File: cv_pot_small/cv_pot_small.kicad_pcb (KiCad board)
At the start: 2 copper layers, 24 x 17 mm, 13 parts, among them J1 I/O connector, U1 HT7550-1, U2 LMV321IDBVR

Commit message: Switched to TLV6001UIDBVR Opamp
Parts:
- U2: value LMV321IDBVR -> TLV6001UIDBVR
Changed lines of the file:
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@@
     (descr "SOT, 5 Pin (https://www.jedec.org/sites/default/files/docs/Mo-178c.PDF variant AA), generated with kicad-footprint-generator ipc_gullwing_generator.py")
     (tags "SOT TO_SOT_SMD")
-    (property "LCSC" "C7972")
+    (property "LCSC" "")
     (property "Sheetfile" "cv_pot_small.kicad_sch")
     (property "Sheetname" "")
@@
       (effects (font (size 1 1) (thickness 0.15)))
     )
-    (fp_text value "LMV321IDBVR" (at 0 2.4 90) (layer "F.Fab")
+    (fp_text value "TLV6001UIDBVR" (at 0 2.4 90) (layer "F.Fab")
       (effects (font (size 1 1) (thickness 0.15)))
     )

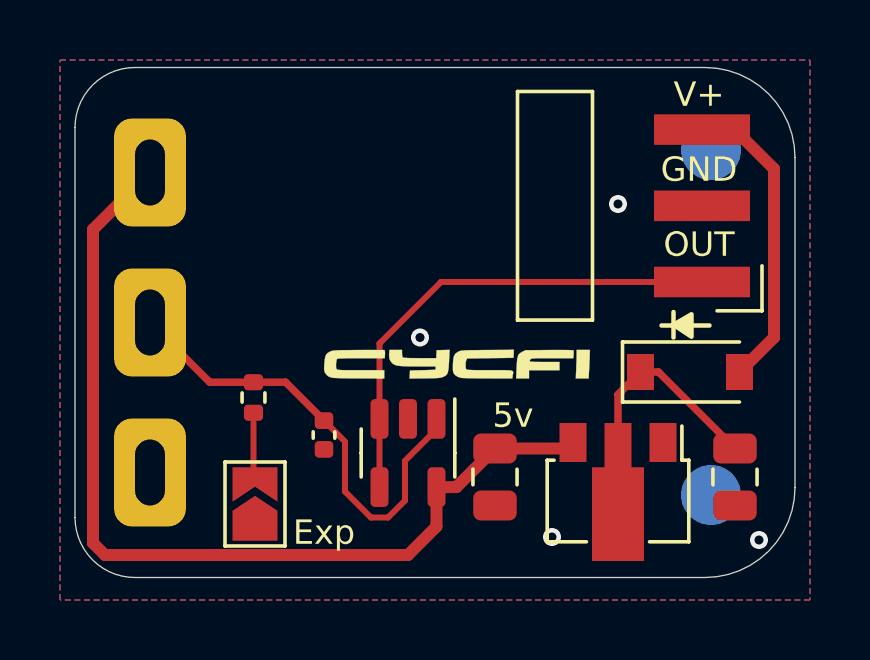
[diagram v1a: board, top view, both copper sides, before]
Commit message: Changed taper resistor value
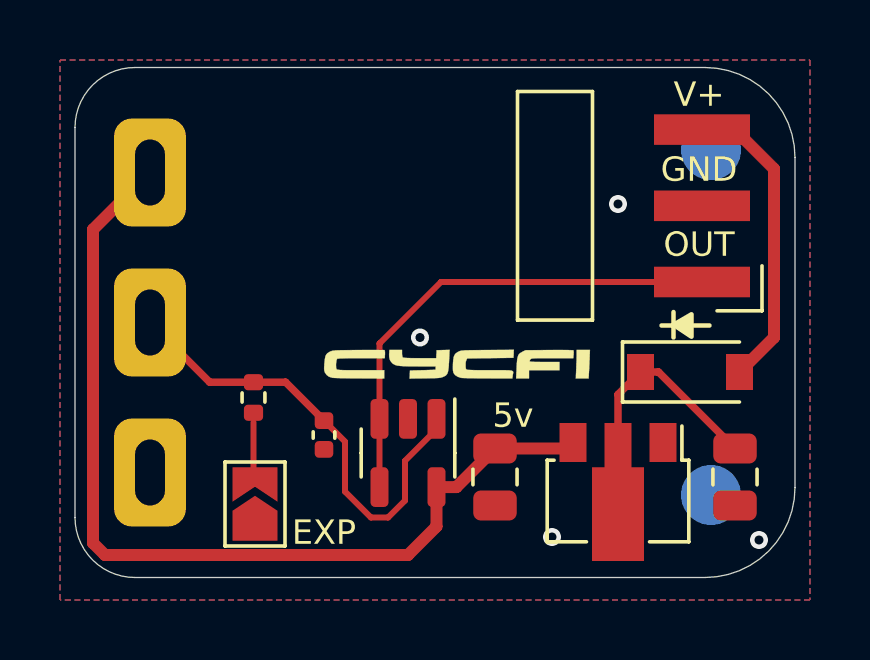
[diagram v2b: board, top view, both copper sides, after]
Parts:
- R1: value 4.7k -> 47k
- RV1: value 25k -> 250k
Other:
- board text added: "EXP"
- board text removed: "Exp"
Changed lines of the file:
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@@
   (footprint "cycfi_library:bourns_pdb181" (layer "F.Cu")
     (at 139.5 75.5)
-    (property "Sheetfile" "cv_pot_small.kicad_sch")
+    (property "Sheetfile" "File: cv_pot_small.kicad_sch")
     (property "Sheetname" "")
     (attr smd)
@@
       (effects (font (size 1 1) (thickness 0.15)))
     )
-    (fp_text value "25k" (at 0 15 unlocked) (layer "F.Fab")
+    (fp_text value "250k" (at 0 15 unlocked) (layer "F.Fab")
       (effects (font (size 1 1) (thickness 0.15)))
     )
@@
   (footprint "cycfi_library:pin_header_1x3p_2.54mm_smd_horizontal" (layer "F.Cu")
     (at 157.9 79.15 180)
-    (property "Sheetfile" "cv_pot_small.kicad_sch")
+    (property "Sheetfile" "File: cv_pot_small.kicad_sch")
     (property "Sheetname" "")
     (attr through_hole)
@@
     (descr "SOT, 5 Pin (https://www.jedec.org/sites/default/files/docs/Mo-178c.PDF variant AA), generated with kicad-footprint-generator ipc_gullwing_generator.py")
     (tags "SOT TO_SOT_SMD")
-    (property "LCSC" "")
-    (property "Sheetfile" "cv_pot_small.kicad_sch")
+    (property "JLCPCB_CORRECTION" "0;0;180")
+    (property "LCSC" "C544299")
+    (property "Sheetfile" "File: cv_pot_small.kicad_sch")
     (property "Sheetname" "")
     (attr smd)
@@
     (tags "capacitor")
     (property "LCSC" "C15850")
-    (property "Sheetfile" "cv_pot_small.kicad_sch")
+    (property "Sheetfile" "File: cv_pot_small.kicad_sch")
     (property "Sheetname" "")
     (attr smd)
@@
     (tags "SOD-123")
     (property "LCSC" "C81598")
-    (property "Sheetfile" "cv_pot_small.kicad_sch")
+    (property "Sheetfile" "File: cv_pot_small.kicad_sch")
     (property "Sheetname" "")
     (attr smd)
@@
     )
   )
-  (footprint "cycfi_library:cycfi-logo-9mm" locked (layer "F.Cu")
+  (footprint "cycfi_library:cycfi-logo-9mm" (layer "F.Cu")
     (at 149.7 81.9)
-    (attr through_hole)
+    (attr through_hole board_only)
     (fp_text reference "G***" (at 0 0) (layer "F.SilkS") hide
       (effects (font (size 1.524 1.524) (thickness 0.3)))
@@
     (descr "SOT-89-3, http://ww1.microchip.com/downloads/en/DeviceDoc/3L_SOT-89_MB_C04-029C.pdf")
     (tags "SOT-89-3")
+    (property "JLCPCB_CORRECTION" "0;0;180")
     (property "LCSC" "C16106")
-    (property "Sheetfile" "cv_pot_small.kicad_sch")
+    (property "Sheetfile" "File: cv_pot_small.kicad_sch")
     (property "Sheetname" "")
     (attr smd)
@@
     (descr "Resistor SMD 0402 (1005 Metric), square (rectangular) end terminal, IPC_7351 nominal, (Body size source: IPC-SM-782 page 72, https://www.pcb-3d.com/wordpress/wp-content/uploads/ipc-sm-782a_amendment_1_and_2.pdf), generated with kicad-footprint-generator")
     (tags "resistor")
-    (property "LCSC" "C25900")
-    (property "Sheetfile" "cv_pot_small.kicad_sch")
+    (property "LCSC" "C25792")
+    (property "Sheetfile" "File: cv_pot_small.kicad_sch")
     (property "Sheetname" "")
     (attr smd)
@@
       (effects (font (size 1 1) (thickness 0.15)))
     )
-    (fp_text value "4.7k" (at 0 1.17 -90) (layer "F.Fab")
+    (fp_text value "47k" (at 0 1.17 -90) (layer "F.Fab")
       (effects (font (size 1 1) (thickness 0.15)))
     )
@@
     (tags "capacitor")
     (property "LCSC" "C15850")
-    (property "Sheetfile" "cv_pot_small.kicad_sch")
+    (property "Sheetfile" "File: cv_pot_small.kicad_sch")
     (property "Sheetname" "")
     (attr smd)
@@
     (tags "capacitor")
     (property "LCSC" "C307331")
-    (property "Sheetfile" "cv_pot_small.kicad_sch")
+    (property "Sheetfile" "File: cv_pot_small.kicad_sch")
     (property "Sheetname" "")
     (attr smd)
@@
     (descr "SMD Solder Jumper, 1x1.5mm Triangular Pads, 0.3mm gap, open")
     (tags "solder jumper open")
-    (property "Sheetfile" "cv_pot_small.kicad_sch")
+    (property "Sheetfile" "File: cv_pot_small.kicad_sch")
     (property "Sheetname" "")
     (attr exclude_from_pos_files)
@@
   (footprint "cycfi_library:single-pad-2x2-circular" (layer "B.Cu")
     (at 158.2 74.75 180)
-    (property "Sheetfile" "cv_pot_small.kicad_sch")
+    (property "Sheetfile" "File: cv_pot_small.kicad_sch")
     (property "Sheetname" "")
     (attr through_hole)
@@
   (footprint "cycfi_library:single-pad-2x2-circular" (layer "B.Cu")
     (at 158.2 86.25 180)
-    (property "Sheetfile" "cv_pot_small.kicad_sch")
+    (property "Sheetfile" "File: cv_pot_small.kicad_sch")
     (property "Sheetname" "")
     (attr through_hole)
@@
   (gr_line (start 158 89) (end 139 89) (layer "Edge.Cuts") (width 0.0381))
   (gr_arc (start 137 74) (mid 137.585786 72.585786) (end 139 72) (layer "Edge.Cuts") (width 0.0381))
-  (gr_text "Exp" (at 145.3 87.5) (layer "F.SilkS")
+  (gr_text "EXP" (at 145.3 87.5) (layer "F.SilkS")
     (effects (font (size 0.8128 0.8128) (thickness 0.1524)))
   )

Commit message: Added 1k output resistor
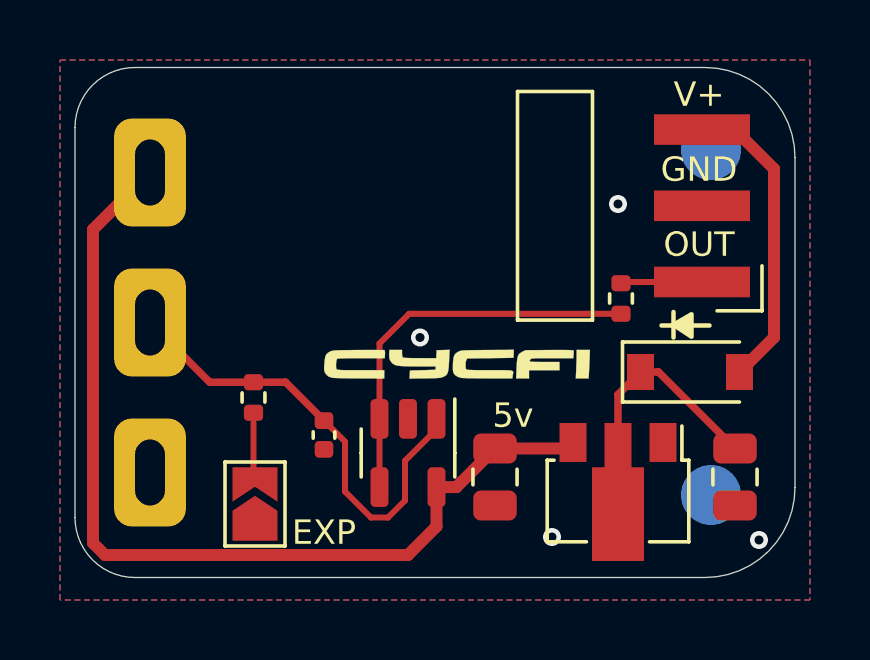
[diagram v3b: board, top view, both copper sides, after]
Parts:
- added R2: 1k, Resistor_SMD:R_0402_1005Metric, F.Cu at (155.2, 79.7)
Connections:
- U2 pad 3: OUT -> Net-(U2-Pad3)
- U2 pad 4: OUT -> Net-(U2-Pad3)
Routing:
- net OUT: track 16.4 -> 2.72 mm
- net Net-(U2-Pad3): track 0.00 -> 13.2 mm
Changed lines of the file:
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@@
   (net 6 "OUT")
   (net 7 "Net-(JP1-Pad2)")
+  (net 8 "Net-(U2-Pad3)")
   (footprint "cycfi_library:bourns_pdb181" (layer "F.Cu")
     (at 139.5 75.5)
@@
       (net 2 "GND") (pinfunction "V-") (pintype "power_in"))
     (pad "3" smd roundrect (at -1.1375 0.95 270) (size 1.325 0.6) (layers "F.Cu" "F.Paste" "F.Mask") (roundrect_rratio 0.25)
-      (net 6 "OUT") (pinfunction "-") (pintype "input"))
+      (net 8 "Net-(U2-Pad3)") (pinfunction "-") (pintype "input"))
     (pad "4" smd roundrect (at 1.1375 0.95 270) (size 1.325 0.6) (layers "F.Cu" "F.Paste" "F.Mask") (roundrect_rratio 0.25)
-      (net 6 "OUT") (pintype "output"))
+      (net 8 "Net-(U2-Pad3)") (pintype "output"))
     (pad "5" smd roundrect (at 1.1375 -0.95 270) (size 1.325 0.6) (layers "F.Cu" "F.Paste" "F.Mask") (roundrect_rratio 0.25)
       (net 3 "5v") (pinfunction "V+") (pintype "power_in"))
@@
     )
   )
+  (footprint "Resistor_SMD:R_0402_1005Metric" (layer "F.Cu")
+    (at 155.2 79.7 90)
+    (descr "Resistor SMD 0402 (1005 Metric), square (rectangular) end terminal, IPC_7351 nominal, (Body size source: IPC-SM-782 page 72, https://www.pcb-3d.com/wordpress/wp-content/uploads/ipc-sm-782a_amendment_1_and_2.pdf), generated with kicad-footprint-generator")
+    (tags "resistor")
+    (property "LCSC" "C11702")
+    (property "Sheetfile" "File: cv_pot_small.kicad_sch")
+    (property "Sheetname" "")
+    (attr smd)
+    (fp_text reference "R2" (at 0 -1.17 90) (layer "F.SilkS") hide
+      (effects (font (size 1 1) (thickness 0.15)))
+    )
+    (fp_text value "1k" (at 0 1.17 90) (layer "F.Fab")
+      (effects (font (size 1 1) (thickness 0.15)))
+    )
+    (fp_text user "${REFERENCE}" (at 0 0 90) (layer "F.Fab")
+      (effects (font (size 0.26 0.26) (thickness 0.04)))
+    )
+    (fp_line (start -0.153641 0.38) (end 0.153641 0.38) (layer "F.SilkS") (width 0.12))
+    (fp_line (start -0.153641 -0.38) (end 0.153641 -0.38) (layer "F.SilkS") (width 0.12))
+    (fp_line (start 0.93 0.47) (end -0.93 0.47) (layer "F.CrtYd") (width 0.05))
+    (fp_line (start -0.93 0.47) (end -0.93 -0.47) (layer "F.CrtYd") (width 0.05))
+    (fp_line (start 0.93 -0.47) (end 0.93 0.47) (layer "F.CrtYd") (width 0.05))
+    (fp_line (start -0.93 -0.47) (end 0.93 -0.47) (layer "F.CrtYd") (width 0.05))
+    (fp_line (start 0.525 0.27) (end -0.525 0.27) (layer "F.Fab") (width 0.1))
+    (fp_line (start 0.525 -0.27) (end 0.525 0.27) (layer "F.Fab") (width 0.1))
+    (fp_line (start -0.525 0.27) (end -0.525 -0.27) (layer "F.Fab") (width 0.1))
+    (fp_line (start -0.525 -0.27) (end 0.525 -0.27) (layer "F.Fab") (width 0.1))
+    (pad "1" smd roundrect (at -0.51 0 90) (size 0.54 0.64) (layers "F.Cu" "F.Paste" "F.Mask") (roundrect_rratio 0.25)
+      (net 8 "Net-(U2-Pad3)") (pintype "passive"))
+    (pad "2" smd roundrect (at 0.51 0 90) (size 0.54 0.64) (layers "F.Cu" "F.Paste" "F.Mask") (roundrect_rratio 0.25)
+      (net 6 "OUT") (pintype "passive"))
+    (model "${KICAD6_3DMODEL_DIR}/Resistor_SMD.3dshapes/R_0402_1005Metric.wrl"
+      (offset (xyz 0 0 0))
+      (scale (xyz 1 1 1))
+      (rotate (xyz 0 0 0))
+    )
+  )
   (footprint "Capacitor_SMD:C_0805_2012Metric" (layer "F.Cu")
     (at 151 85.65 -90)
@@
   (segment (start 160.3 81) (end 159.15 82.15) (width 0.4) (layer "F.Cu") (net 5))
   (segment (start 157.9 74.07) (end 158.99 74.07) (width 0.4) (layer "F.Cu") (net 5))
-  (segment (start 147.15 85.9875) (end 147.15 83.7125) (width 0.2) (layer "F.Cu") (net 6))
-  (segment (start 147.15 81.2) (end 149.2 79.15) (width 0.2) (layer "F.Cu") (net 6))
-  (segment (start 147.15 83.7125) (end 147.15 81.2) (width 0.2) (layer "F.Cu") (net 6))
-  (segment (start 149.2 79.15) (end 157.9 79.15) (width 0.2) (layer "F.Cu") (net 6))
+  (segment (start 157.9 79.15) (end 155.24 79.15) (width 0.2032) (layer "F.Cu") (net 6))
+  (segment (start 155.24 79.15) (end 155.2 79.19) (width 0.2032) (layer "F.Cu") (net 6))
   (segment (start 142.95 85.775) (end 143 85.825) (width 0.2) (layer "F.Cu") (net 7))
   (segment (start 142.95 83.825) (end 142.95 85.775) (width 0.2) (layer "F.Cu") (net 7))
+  (segment (start 147.15 85.9875) (end 147.15 83.7125) (width 0.2) (layer "F.Cu") (net 8))
+  (segment (start 148.14 80.21) (end 147.15 81.2) (width 0.2032) (layer "F.Cu") (net 8))
+  (segment (start 147.15 83.7125) (end 147.15 81.2) (width 0.2) (layer "F.Cu") (net 8))
+  (segment (start 155.2 80.21) (end 148.14 80.21) (width 0.2032) (layer "F.Cu") (net 8))
   (zone (net 2) (net_name "GND") (layer "F.Cu") (hatch edge 0.508)
     (connect_pads (clearance 0.3))
